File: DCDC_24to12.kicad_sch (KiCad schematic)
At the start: 26 parts, among them J1 Power_IN, J2 Power_OUT, U1 BD9F800MUX-ZE2

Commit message: 穴追加
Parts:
- added H1, H2: MountingHole_Pad, MountingHole:MountingHole_3.2mm_M3_Pad_Via, symbol Mechanical:MountingHole_Pad
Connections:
- no-connect marks 0 -> 2
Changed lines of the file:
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@@
 		(color 0 0 0 0)
+	)
+	(no_connect
+		(at 200.66 143.51)
+	)
+	(no_connect
+		(at 172.72 143.51)
 	)
 	(wire
@@
 	)
 	(symbol
+		(lib_id "Mechanical:MountingHole_Pad")
+		(at 172.72 140.97 0)
+		(unit 1)
+		(exclude_from_sim yes)
+		(in_bom no)
+		(on_board yes)
+		(dnp no)
+		(fields_autoplaced yes)
+		(property "Reference" "H1"
+			(at 175.26 138.4299 0)
+			(effects
+				(font
+					(size 1.27 1.27)
+				)
+				(justify left)
+			)
+		)
+		(property "Value" "MountingHole_Pad"
+			(at 175.26 140.9699 0)
+			(effects
+				(font
+					(size 1.27 1.27)
+				)
+				(justify left)
+			)
+		)
+		(property "Footprint" "MountingHole:MountingHole_3.2mm_M3_Pad_Via"
+			(at 172.72 140.97 0)
+			(effects
+				(font
+					(size 1.27 1.27)
+				)
+				(hide yes)
+			)
+		)
+		(property "Datasheet" "~"
+			(at 172.72 140.97 0)
+			(effects
+				(font
+					(size 1.27 1.27)
+				)
+				(hide yes)
+			)
+		)
+		(property "Description" "Mounting Hole with connection"
+			(at 172.72 140.97 0)
+			(effects
+				(font
+					(size 1.27 1.27)
+				)
+				(hide yes)
+			)
+		)
+		(pin "1"
+		)
+		(instances
+			(project ""
+				(path "/9b31bb12-b0a4-46c2-8fe3-73cecf9f3124"
+					(reference "H1")
+					(unit 1)
+				)
+			)
+		)
+	)
+	(symbol
 		(lib_id "power:+BATT")
 		(at 140.97 90.17 0)
@@
 					(unit 1)
 				)
+			)
+		)
+	)
+	(symbol
+		(lib_id "Mechanical:MountingHole_Pad")
+		(at 200.66 140.97 0)
+		(unit 1)
+		(exclude_from_sim yes)
+		(in_bom no)
+		(on_board yes)
+		(dnp no)
+		(fields_autoplaced yes)
+		(property "Reference" "H2"
+			(at 203.2 138.4299 0)
+			(effects
+				(font
+					(size 1.27 1.27)
+				)
+				(justify left)
+			)
+		)
+		(property "Value" "MountingHole_Pad"
+			(at 203.2 140.9699 0)
+			(effects
+				(font
+					(size 1.27 1.27)
+				)
+				(justify left)
+			)
+		)
+		(property "Footprint" "MountingHole:MountingHole_3.2mm_M3_Pad_Via"
+			(at 200.66 140.97 0)
+			(effects
+				(font
+					(size 1.27 1.27)
+				)
+				(hide yes)
+			)
+		)
+		(property "Datasheet" "~"
+			(at 200.66 140.97 0)
+			(effects
+				(font
+					(size 1.27 1.27)
+				)
+				(hide yes)
+			)
+		)
+		(property "Description" "Mounting Hole with connection"
+			(at 200.66 140.97 0)
+			(effects
+				(font
+					(size 1.27 1.27)
+				)
+				(hide yes)
+			)
+		)
+		(pin "1"
+		)
+		(instances
+			(project ""
+				(path "/9b31bb12-b0a4-46c2-8fe3-73cecf9f3124"
+					(reference "H2")
+					(unit 1)
+				)

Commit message: 出力コネクタをタテにした
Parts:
- J2: footprint Connector_AMASS:AMASS_XT60PW-F_1x02_P7.20mm_Horizontal -> Connector_AMASS:AMASS_XT60-F_1x02_P7.20mm_Vertical
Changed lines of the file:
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@@
 			)
 		)
-		(property "Footprint" "Connector_AMASS:AMASS_XT60PW-F_1x02_P7.20mm_Horizontal"
+		(property "Footprint" "Connector_AMASS:AMASS_XT60-F_1x02_P7.20mm_Vertical"
 			(at 173.99 81.28 0)
 			(effects

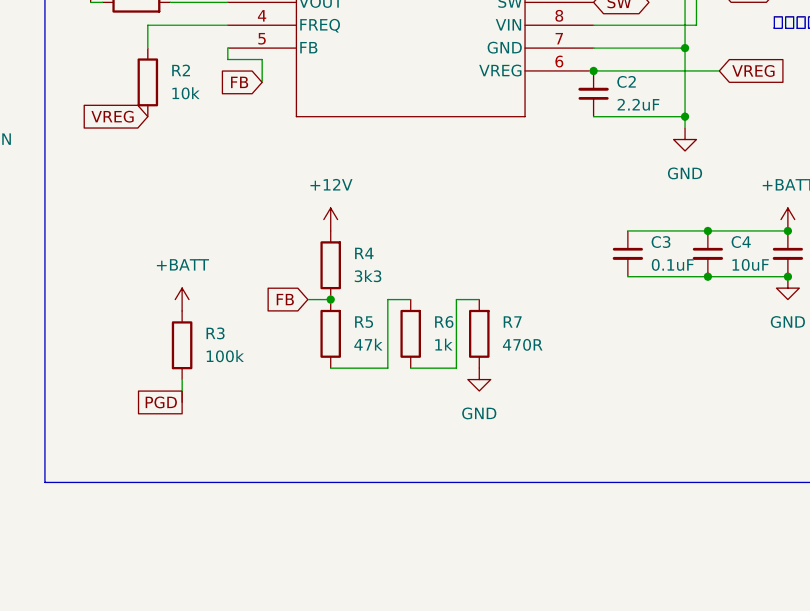
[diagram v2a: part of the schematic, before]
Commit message: フィードバック抵抗上下逆だったので修正
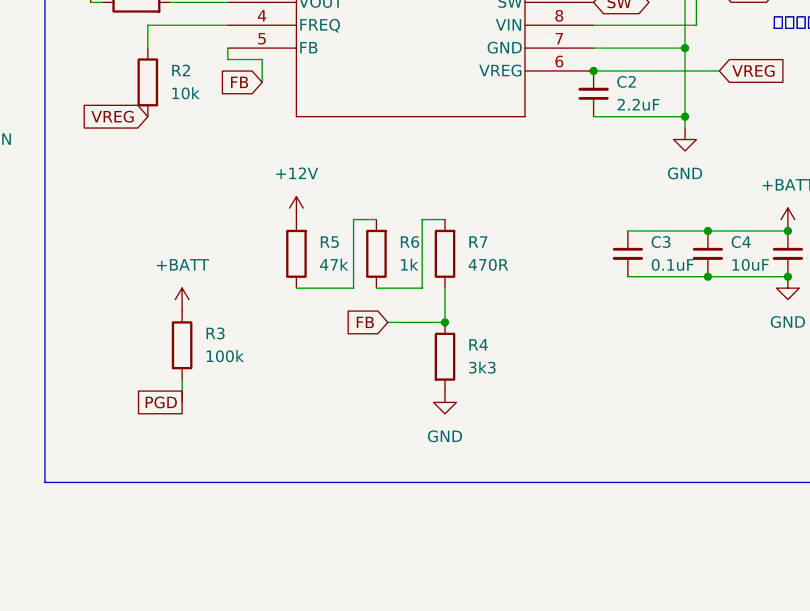
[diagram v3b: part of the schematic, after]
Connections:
- net +12V: now also R5.2; no longer R4.2
- net FB: now also R7.1; no longer R5.2
- net GND: now also R4.2; no longer R7.1
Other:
- moved on the sheet: R4, R5, R6, R7
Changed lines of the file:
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@@
 	)
 	(junction
+		(at 102.87 100.33)
+		(diameter 0)
+		(color 0 0 0 0)
+	)
+	(junction
 		(at 129.54 77.47)
 		(diameter 0)
@@
 		(color 0 0 0 0)
 	)
-	(junction
-		(at 90.17 97.79)
-		(diameter 0)
-		(color 0 0 0 0)
-	)
 	(no_connect
 		(at 200.66 143.51)
@@
 	(wire
 		(pts
+			(xy 102.87 96.52) (xy 102.87 100.33)
+		)
+		(stroke
+			(width 0)
+			(type default)
+		)
+	)
+	(wire
+		(pts
 			(xy 36.83 76.2) (xy 45.72 76.2)
 		)
@@
 	(wire
 		(pts
-			(xy 96.52 105.41) (xy 96.52 97.79)
+			(xy 92.71 96.52) (xy 92.71 88.9)
 		)
 		(stroke
@@
 	(wire
 		(pts
-			(xy 90.17 105.41) (xy 96.52 105.41)
+			(xy 86.36 96.52) (xy 92.71 96.52)
 		)
 		(stroke
@@
 	(wire
 		(pts
-			(xy 96.52 97.79) (xy 99.06 97.79)
+			(xy 92.71 88.9) (xy 95.25 88.9)
 		)
 		(stroke
@@
 	(wire
 		(pts
-			(xy 99.06 105.41) (xy 104.14 105.41)
+			(xy 95.25 96.52) (xy 100.33 96.52)
 		)
 		(stroke
@@
 	(wire
 		(pts
-			(xy 104.14 105.41) (xy 104.14 97.79)
+			(xy 100.33 96.52) (xy 100.33 88.9)
 		)
 		(stroke
@@
 	(wire
 		(pts
-			(xy 87.63 97.79) (xy 90.17 97.79)
+			(xy 129.54 62.23) (xy 129.54 69.85)
 		)
 		(stroke
@@
 	(wire
 		(pts
-			(xy 129.54 62.23) (xy 129.54 69.85)
+			(xy 96.52 100.33) (xy 102.87 100.33)
 		)
 		(stroke
@@
 	(wire
 		(pts
-			(xy 104.14 97.79) (xy 106.68 97.79)
+			(xy 100.33 88.9) (xy 102.87 88.9)
 		)
 		(stroke
@@
 	(global_label "FB"
 		(shape input)
-		(at 87.63 97.79 180)
+		(at 96.52 100.33 180)
 		(effects
 			(font
@@
 		)
 		(property "Intersheetrefs" "${INTERSHEET_REFS}"
-			(at 87.63 97.79 0)
+			(at 96.52 100.33 0)
 			(effects
 				(font
@@
 	(symbol
 		(lib_id "power:GND")
-		(at 106.68 105.41 0)
+		(at 102.87 107.95 0)
 		(unit 1)
 		(exclude_from_sim no)
@@
 		(dnp no)
 		(property "Reference" "#PWR06"
-			(at 106.68 111.76 0)
+			(at 102.87 114.3 0)
 			(effects
 				(font
@@
 		)
 		(property "Value" "GND"
-			(at 106.68 110.49 0)
+			(at 102.87 113.03 0)
 			(effects
 				(font
@@
 		)
 		(property "Footprint" ""
-			(at 106.68 105.41 0)
+			(at 102.87 107.95 0)
 			(effects
 				(font
@@
 		)
 		(property "Datasheet" ""
-			(at 106.68 105.41 0)
+			(at 102.87 107.95 0)
 			(effects
 				(font
@@
 		)
 		(property "Description" "Power symbol creates a global label with name \"GND\" , ground"
-			(at 106.68 105.41 0)
+			(at 102.87 107.95 0)
 			(effects
 				(font
@@
 	(symbol
 		(lib_id "Device:R")
-		(at 90.17 101.6 180)
+		(at 86.36 92.71 180)
 		(unit 1)
 		(exclude_from_sim no)
@@
 		(fields_autoplaced yes)
 		(property "Reference" "R5"
-			(at 92.71 100.3299 0)
+			(at 88.9 91.4399 0)
 			(effects
 				(font
@@
 		)
 		(property "Value" "47k"
-			(at 92.71 102.8699 0)
+			(at 88.9 93.9799 0)
 			(effects
 				(font
@@
 		)
 		(property "Footprint" "Resistor_SMD:R_0805_2012Metric"
-			(at 91.948 101.6 90)
+			(at 88.138 92.71 90)
 			(effects
 				(font
@@
 		)
 		(property "Datasheet" "~"
-			(at 90.17 101.6 0)
+			(at 86.36 92.71 0)
 			(effects
 				(font
@@
 		)
 		(property "Description" "Resistor"
-			(at 90.17 101.6 0)
+			(at 86.36 92.71 0)
 			(effects
 				(font
@@
 	(symbol
 		(lib_id "power:+12V")
-		(at 90.17 90.17 0)
+		(at 86.36 88.9 0)
 		(unit 1)
 		(exclude_from_sim no)
@@
 		(fields_autoplaced yes)
 		(property "Reference" "#PWR05"
-			(at 90.17 93.98 0)
+			(at 86.36 92.71 0)
 			(effects
 				(font
@@
 		)
 		(property "Value" "+12V"
-			(at 90.17 85.09 0)
+			(at 86.36 83.82 0)
 			(effects
 				(font
@@
 		)
 		(property "Footprint" ""
-			(at 90.17 90.17 0)
+			(at 86.36 88.9 0)
 			(effects
 				(font
@@
 		)
 		(property "Datasheet" ""
-			(at 90.17 90.17 0)
+			(at 86.36 88.9 0)
 			(effects
 				(font
@@
 		)
 		(property "Description" "Power symbol creates a global label with name \"+12V\""
-			(at 90.17 90.17 0)
+			(at 86.36 88.9 0)
 			(effects
 				(font
@@
 	(symbol
 		(lib_id "Device:R")
-		(at 106.68 101.6 180)
+		(at 102.87 92.71 180)
 		(unit 1)
 		(exclude_from_sim no)
@@
 		(fields_autoplaced yes)
 		(property "Reference" "R7"
-			(at 109.22 100.3299 0)
+			(at 105.41 91.4399 0)
 			(effects
 				(font
@@
 		)
 		(property "Value" "470R"
-			(at 109.22 102.8699 0)
+			(at 105.41 93.9799 0)
 			(effects
 				(font
@@
 		)
 		(property "Footprint" "Resistor_SMD:R_0805_2012Metric"
-			(at 108.458 101.6 90)
+			(at 104.648 92.71 90)
 			(effects
 				(font
@@
 		)
 		(property "Datasheet" "~"
-			(at 106.68 101.6 0)
+			(at 102.87 92.71 0)
 			(effects
 				(font
@@
 		)
 		(property "Description" "Resistor"
-			(at 106.68 101.6 0)
+			(at 102.87 92.71 0)
 			(effects
 				(font
@@
 	(symbol
 		(lib_id "Device:R")
-		(at 99.06 101.6 180)
+		(at 95.25 92.71 180)
 		(unit 1)
 		(exclude_from_sim no)
@@
 		(fields_autoplaced yes)
 		(property "Reference" "R6"
-			(at 101.6 100.3299 0)
+			(at 97.79 91.4399 0)
 			(effects
 				(font
@@
 		)
 		(property "Value" "1k"
-			(at 101.6 102.8699 0)
+			(at 97.79 93.9799 0)
 			(effects
 				(font
@@
 		)
 		(property "Footprint" "Resistor_SMD:R_0805_2012Metric"
-			(at 100.838 101.6 90)
+			(at 97.028 92.71 90)
 			(effects
 				(font
@@
 		)
 		(property "Datasheet" "~"
-			(at 99.06 101.6 0)
+			(at 95.25 92.71 0)
 			(effects
 				(font
@@
 		)
 		(property "Description" "Resistor"
-			(at 99.06 101.6 0)
+			(at 95.25 92.71 0)
 			(effects
 				(font
@@
 	(symbol
 		(lib_id "Device:R")
-		(at 90.17 93.98 180)
+		(at 102.87 104.14 0)
 		(unit 1)
 		(exclude_from_sim no)
@@
 		(fields_autoplaced yes)
 		(property "Reference" "R4"
-			(at 92.71 92.7099 0)
+			(at 105.41 102.8699 0)
 			(effects
 				(font
 					(size 1.27 1.27)
 				)
-				(justify right)
+				(justify left)
 			)
 		)
 		(property "Value" "3k3"
-			(at 92.71 95.2499 0)
+			(at 105.41 105.4099 0)
 			(effects
 				(font
 					(size 1.27 1.27)
 				)
-				(justify right)
+				(justify left)
 			)
 		)
 		(property "Footprint" "Resistor_SMD:R_0805_2012Metric"
-			(at 91.948 93.98 90)
+			(at 101.092 104.14 90)
 			(effects
 				(font
@@
 		)
 		(property "Datasheet" "~"
-			(at 90.17 93.98 0)
+			(at 102.87 104.14 0)
 			(effects
 				(font
@@
 		)
 		(property "Description" "Resistor"
-			(at 90.17 93.98 0)
+			(at 102.87 104.14 0)
 			(effects
 				(font

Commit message: 再アノテーション
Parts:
- renumbered R5 to R4, R6 to R5, R7 to R6, R4 to R7
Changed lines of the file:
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@@
 		(dnp no)
 		(fields_autoplaced yes)
-		(property "Reference" "R5"
+		(property "Reference" "R4"
 			(at 88.9 91.4399 0)
 			(effects
@@
 			(project "Pi_Header"
 				(path "/9b31bb12-b0a4-46c2-8fe3-73cecf9f3124"
-					(reference "R5")
+					(reference "R4")
 					(unit 1)
 				)
@@
 		(dnp no)
 		(fields_autoplaced yes)
-		(property "Reference" "R7"
+		(property "Reference" "R6"
 			(at 105.41 91.4399 0)
 			(effects
@@
 			(project "DCDC_24to12"
 				(path "/9b31bb12-b0a4-46c2-8fe3-73cecf9f3124"
-					(reference "R7")
+					(reference "R6")
 					(unit 1)
 				)
@@
 		(dnp no)
 		(fields_autoplaced yes)
-		(property "Reference" "R6"
+		(property "Reference" "R5"
 			(at 97.79 91.4399 0)
 			(effects
@@
 			(project "Pi_Header"
 				(path "/9b31bb12-b0a4-46c2-8fe3-73cecf9f3124"
-					(reference "R6")
+					(reference "R5")
 					(unit 1)
 				)
@@
 		(dnp no)
 		(fields_autoplaced yes)
-		(property "Reference" "R4"
+		(property "Reference" "R7"
 			(at 105.41 102.8699 0)
 			(effects
@@
 			(project "Pi_Header"
 				(path "/9b31bb12-b0a4-46c2-8fe3-73cecf9f3124"
-					(reference "R4")
-					(unit 1)
-				)
+					(reference "R7")
+					(unit 1)
+				)
